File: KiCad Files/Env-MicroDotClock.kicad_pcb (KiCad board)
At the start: 2 copper layers, 90 x 65.2 mm, 40 parts, among them IC1 IS31FL3730-QFLS2-TR, IC2 IS31FL3730-QFLS2-TR, IC3 IS31FL3730-QFLS2-TR, IC4 IS31FL3730-QFLS2-TR, M1 LTP-305G, M2 LTP-305G, M3 LTP-305G, M4 LTP-305G, M5 LTP-305G, M6 LTP-305G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

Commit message: small changes and fixes, among other adjustments.
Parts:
- removed U2: DS1307Z+, Package_SO:SOIC-8_3.9x4.9mm_P1.27mm
- removed Y1: 32.768kHz 45kΩ 12.5, Crystal:Crystal_SMD_3225-4Pin_3.2x2.5mm_HandSoldering
- added U3: DS3231M, Package_SO:SOIC-16W_7.5x10.3mm_P1.27mm, F.Cu at (160.7, 115.2)
- BZ1: value PS1240 -> Buzzer
- C10: value 0805 22pf -> 0805 1uF
- C9: value 0805 22pf -> 0805 0.1uF
- Q1: footprint Package_TO_SOT_THT:TO-92_Inline -> Package_TO_SOT_SMD:SOT-23
- moved R2 8.54 mm to (150.1, 121.2), turned to 0 degrees
- moved R1 8.54 mm to (150.1, 119.2), turned to 0 degrees
- moved C9 6.10 mm to (167.6, 117.4)
- moved C10 2.02 mm to (169.7, 116.4), turned to 90 degrees
- moved Q1 1.29 mm to (146.8, 103.4), turned to -90 degrees
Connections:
- C10 pad 1: GND -> +5V
- C10 pad 2: Net-(U2-X2) -> GND
- C9 pad 1: GND -> +5V
- C9 pad 2: Net-(U2-X1) -> GND
- Q1 pad 1: GND -> Net-(Q1-B)
- Q1 pad 2: Net-(BZ1-+) -> GND
- Q1 pad 3: Net-(Q1-B) -> Net-(BZ1-+)
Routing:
- net +5V: track 259.4 -> 282.3 mm
- net I2C_SDA: track 181.5 -> 169.2 mm, vias 6 -> 5
- net Net-(U2-X1): track 7.83 -> 0.00 mm
- net Net-(U2-X2): track 6.93 -> 0.00 mm
- net Net-(BT1-+): track 34.6 -> 41.0 mm
- net I2C_SCL: track 202.8 -> 208.1 mm, vias 6 -> 5
- net Net-(Q1-B): track 2.71 -> 3.48 mm
- net Net-(BZ1-+): track 15.7 -> 14.9 mm
- net GND: vias 71 -> 67

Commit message: some fixes and adjustments.
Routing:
- net I2C_SDA: track 169.2 -> 193.9 mm
- net GND: track 55.6 -> 46.8 mm
- net IC4R1: track 31.3 -> 33.8 mm
- net I2C_SCL: track 208.1 -> 205.9 mm
- net Buzzer GPIO: track 53.8 -> 55.5 mm
- net IC4R3: track 39.2 -> 40.7 mm
- net IC2R4: track 33.6 -> 35.1 mm
- net GPIO5: track 7.66 -> 8.98 mm
- net IC4R4: track 36.0 -> 37.1 mm
- net +5V: track 282.3 -> 283.3 mm
- net IC4C6: track 38.7 -> 39.5 mm
- net IC3R4: track 35.1 -> 35.7 mm
- net IC2C3: track 64.8 -> 65.5 mm
- net IC3R6: track 21.8 -> 22.4 mm
- net IC2C4: track 39.7 -> 40.3 mm
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
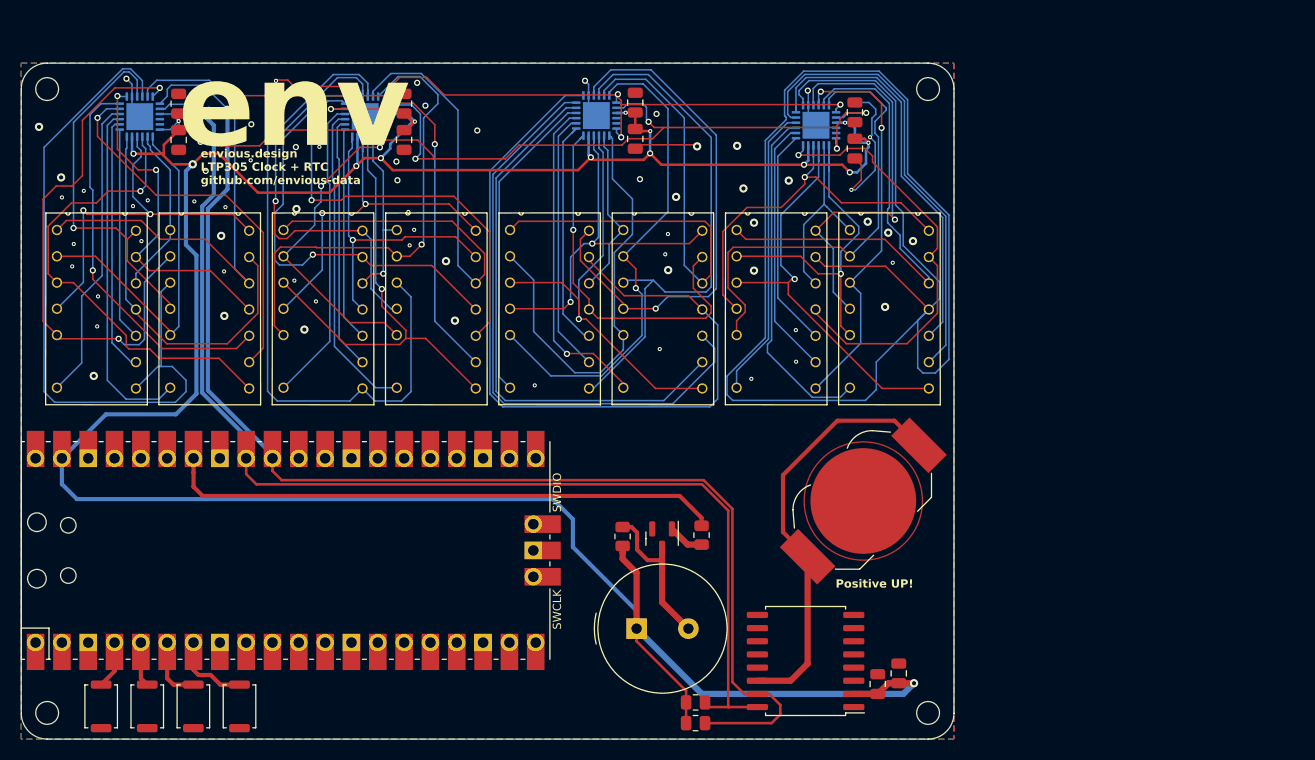
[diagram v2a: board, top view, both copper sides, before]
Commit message: Moved LTP305s up and the matrix ICs below the LTP305s
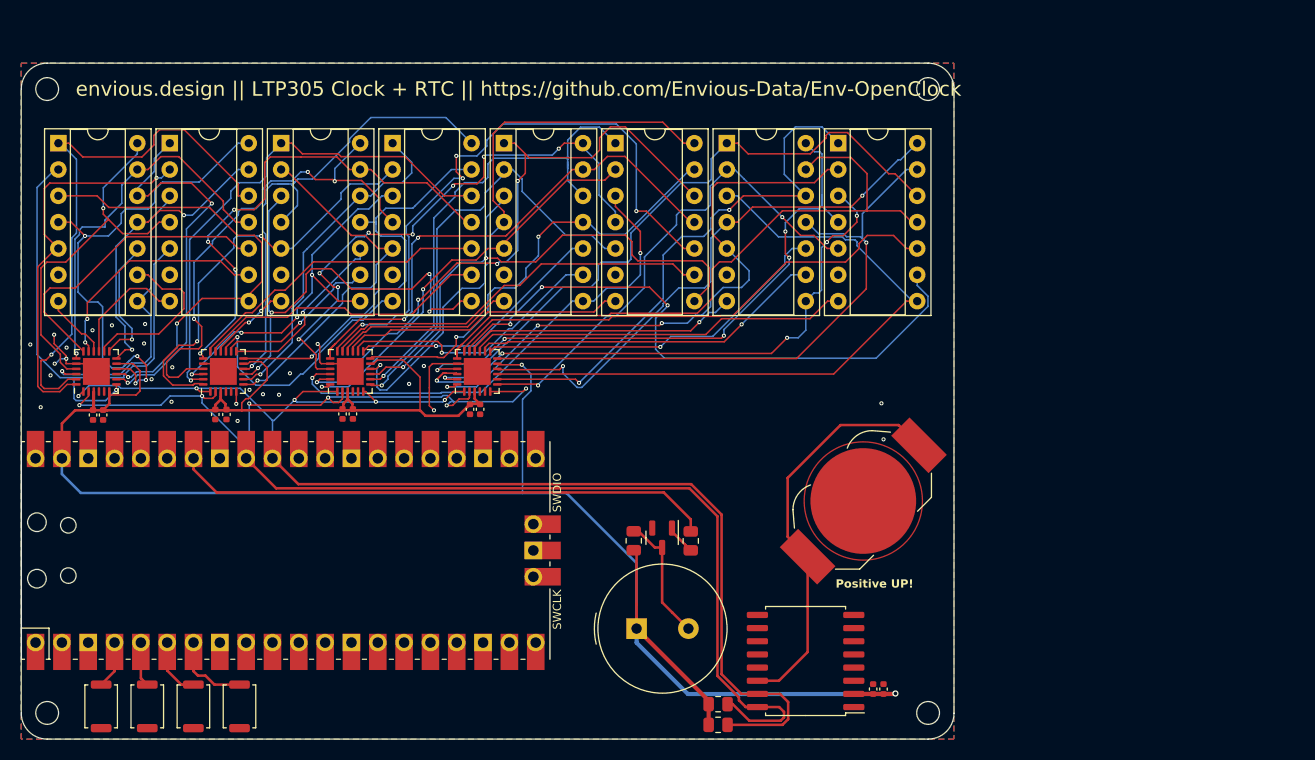
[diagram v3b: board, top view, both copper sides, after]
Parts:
- C1, C3, C5, C7, C9: value 0805 0.1uF -> 0402 0.1uF; footprint Capacitor_SMD:C_0805_2012Metric -> Capacitor_SMD:C_0402_1005Metric
- C10, C2, C4, C6, C8: value 0805 1uF -> 0402 1uF; footprint Capacitor_SMD:C_0805_2012Metric -> Capacitor_SMD:C_0402_1005Metric
- IC1, IC2, IC3, IC4: moved to F.Cu
- M1, M2, M3, M4, M5, M6, M7, M8: footprint LTP-305G:LTP-305G -> Package_DIP:DIP-14_W7.62mm_Socket
- moved C7 46.9 mm to (128.3, 90.9), turned to -90 degrees
- moved C8 44.1 mm to (129.3, 90.9)
- moved C6 40.6 mm to (117.0, 91.3), turned to -90 degrees
- moved IC4 40.4 mm to (129.0, 87.2), turned to 90 degrees
- moved C5 38.8 mm to (116.0, 91.3)
- moved C4 34.5 mm to (104.8, 91.4), turned to -90 degrees
- moved IC3 34.3 mm to (116.8, 87.2), turned to 90 degrees
- moved C3 32.1 mm to (103.7, 91.4)
- moved C2 30.9 mm to (92.9, 91.5), turned to -90 degrees
- moved IC2 28.1 mm to (104.5, 87.2), turned to 90 degrees
- moved C1 27.8 mm to (91.9, 91.5)
- moved IC1 24.9 mm to (92.2, 87.2), turned to 90 degrees
- moved M8 16.7 mm to (163.8, 65.2)
- moved M7 16.6 mm to (153.1, 65.2)
- moved M6 16.6 mm to (142.3, 65.2)
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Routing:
- net IC4C5: track 154.8 -> 66.4 mm
- net I2C_SDA: track 193.9 -> 130.3 mm
- net I2C_SCL: track 205.9 -> 144.3 mm, vias 5 -> 6
- net +5V: track 283.3 -> 228.6 mm, vias 15 -> 2
- net IC1C3: track 68.6 -> 28.5 mm, vias 0 -> 1
- net IC4R2: track 18.1 -> 53.2 mm, vias 0 -> 2
- net IC3R2: track 16.9 -> 47.7 mm, vias 0 -> 1
- net IC2C3: track 65.5 -> 36.1 mm, vias 0 -> 4
- net IC3C5: track 78.8 -> 52.5 mm, vias 0 -> 2
- net IC4R3: track 40.7 -> 66.2 mm, vias 1 -> 0
- net IC1C8: track 29.4 -> 6.47 mm
- net IC1R8: track 33.3 -> 11.7 mm
- net IC2C8: track 29.5 -> 8.10 mm, vias 0 -> 2
- net IC1R2: track 16.4 -> 37.8 mm, vias 0 -> 2
- net GND: track 46.8 -> 25.9 mm, vias 67 -> 26
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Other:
- board text added: "envious.design || LTP305 Clock + RTC || https://github.com/Envious-Data/Env-OpenClock"
- board text removed: "envious.design LTP305 Clock + RTC github.com/envious-data"

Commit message: updated production files
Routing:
- net IC2R4: track 48.9 -> 51.7 mm
- net I2C_SDA: track 130.3 -> 131.3 mm
- net IC2C6: track 29.5 -> 30.3 mm
- net IC3R2: track 47.7 -> 47.0 mm
- net I2C_SCL: track 144.3 -> 145.0 mm
- net IC3C7: track 38.1 -> 38.6 mm

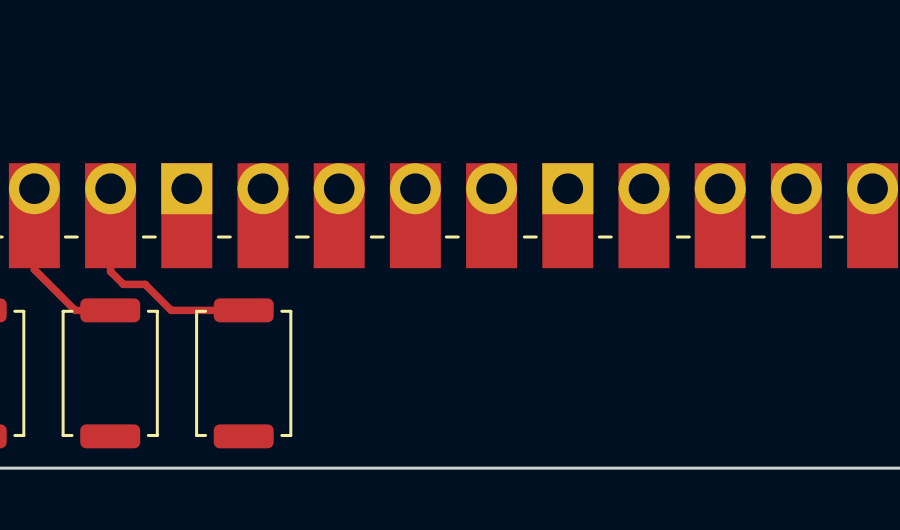
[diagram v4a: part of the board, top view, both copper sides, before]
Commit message: added dip switch for summer time adjustment
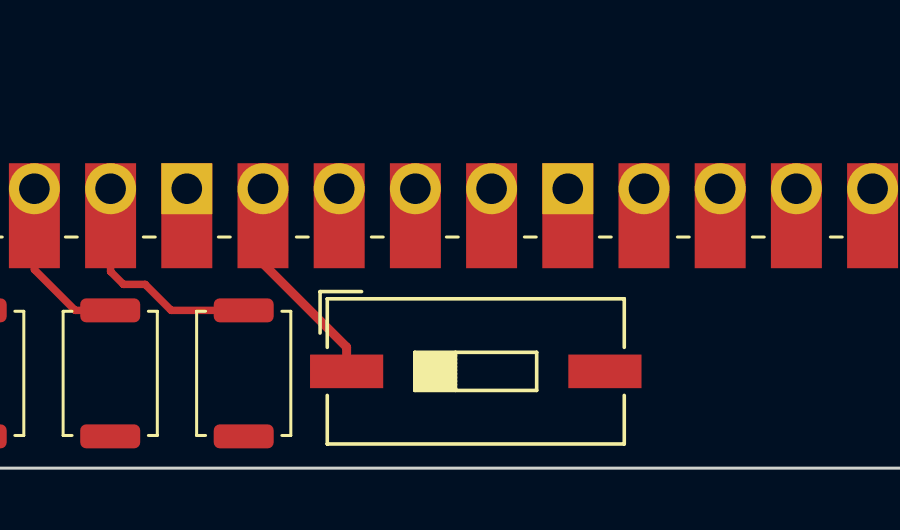
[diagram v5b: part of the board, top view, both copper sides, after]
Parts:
- added SW5: DIP SPST, Button_Switch_SMD:SW_DIP_SPSTx01_Slide_9.78x4.72mm_W8.61mm_P2.54mm, F.Cu at (113.8, 119.5)
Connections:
- U1 pad 9: unconnected-(U1-GPIO6-Pad9) -> GPIO6
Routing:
- net GPIO6: track 0.00 -> 7.24 mm

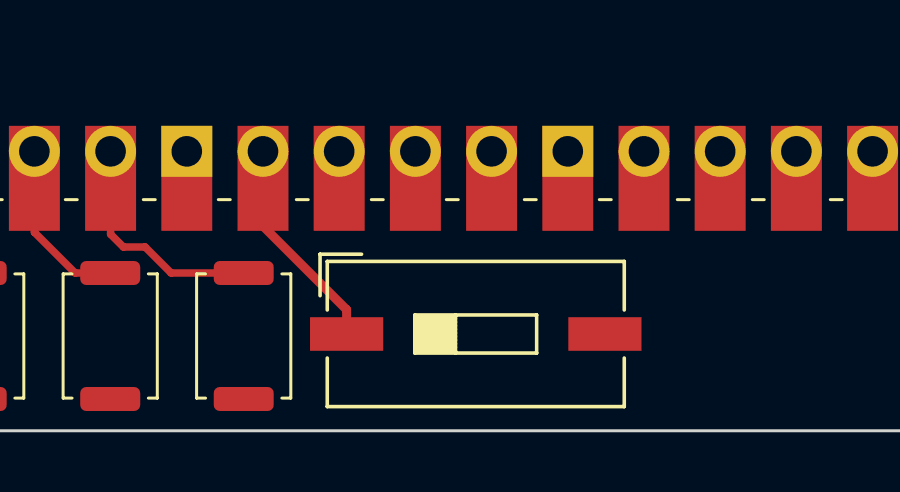
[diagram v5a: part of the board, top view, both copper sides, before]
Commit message: swapped dipswitch for smaller
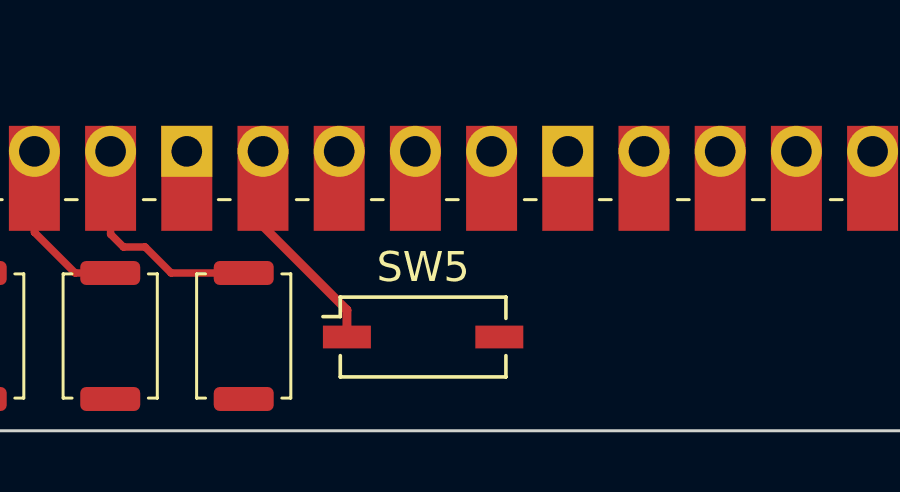
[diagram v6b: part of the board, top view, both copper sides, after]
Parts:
- SW5: footprint Button_Switch_SMD:SW_DIP_SPSTx01_Slide_9.78x4.72mm_W8.61mm_P2.54mm -> Button_Switch_SMD:SW_DIP_SPSTx01_Slide_Copal_CHS-01A_W5.08mm_P1.27mm_JPin
- moved SW5 1.76 mm to (112.0, 119.6)
